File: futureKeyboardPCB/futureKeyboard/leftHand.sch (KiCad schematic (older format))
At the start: 56 parts, among them J10 Conn_01x02, J11 Conn_01x01, J12 Conn_01x01, J13 Conn_01x04, J14 Conn_01x06, J15 Conn_01x06, J16 Conn_01x01, J9 Conn_01x01, P3 CONN_01X02, P4 CONN_01X06, Q4 2SC1815, Q5 2SC1815, Q6 2SC1815, SW10 SW_Push, SW11 SW_Push, SW12 SW_Push, SW13 SW_Push, SW14 SW_Push, SW15 SW_Push, SW16 SW_Push, SW17 SW_Push, SW18 SW_Push, SW19 SW_Push, SW20 SW_Push, SW21 SW_Push, SW22 SW_Push, SW23 SW_Push, SW24 SW_Push, SW25 SW_Push, SW9 SW_SPDT, U3 AMS1117-1.5, U4 ESP32

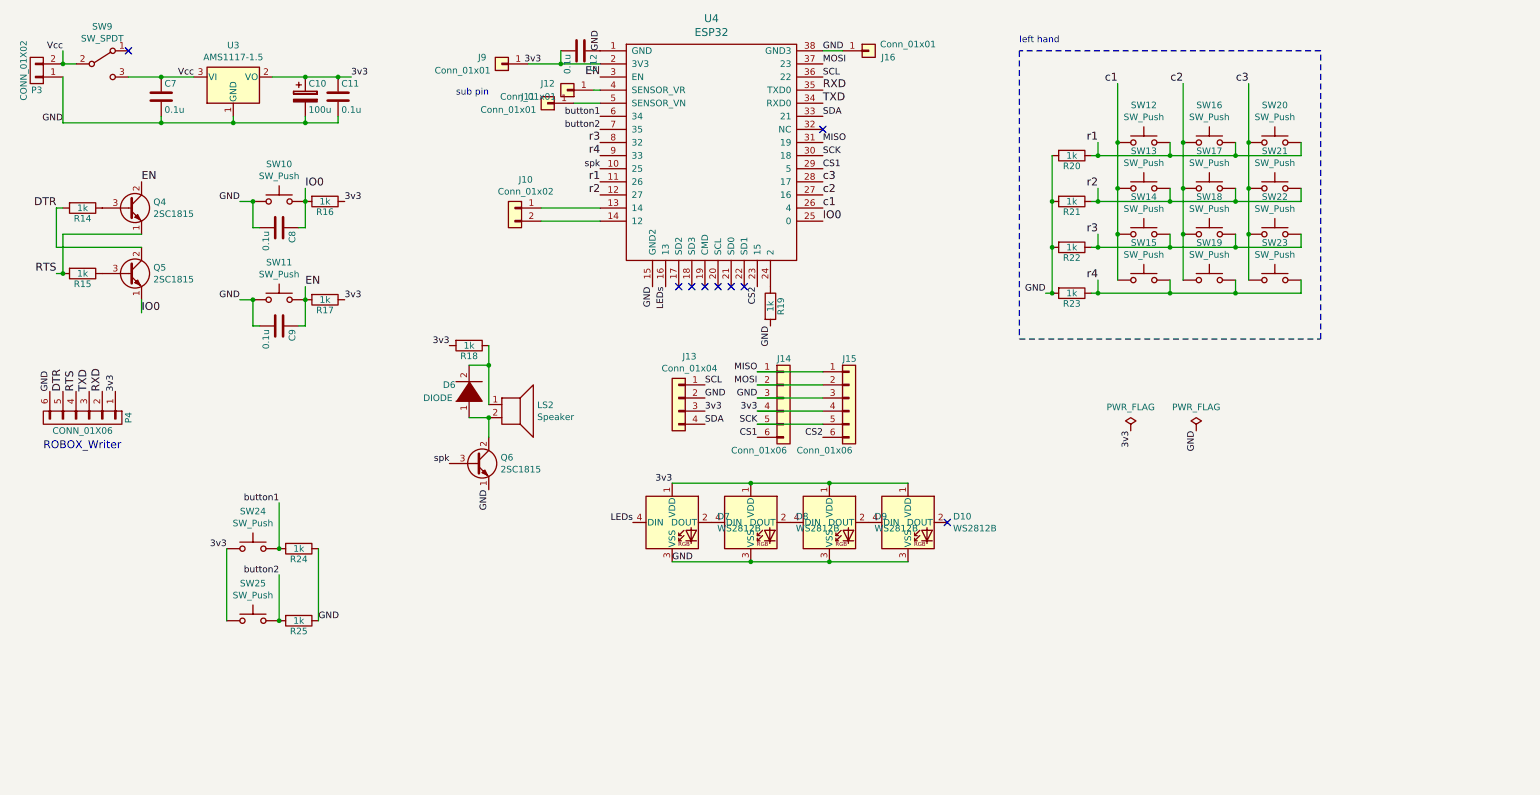
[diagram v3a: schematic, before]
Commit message: divide layors, make footprints, aligned footprints
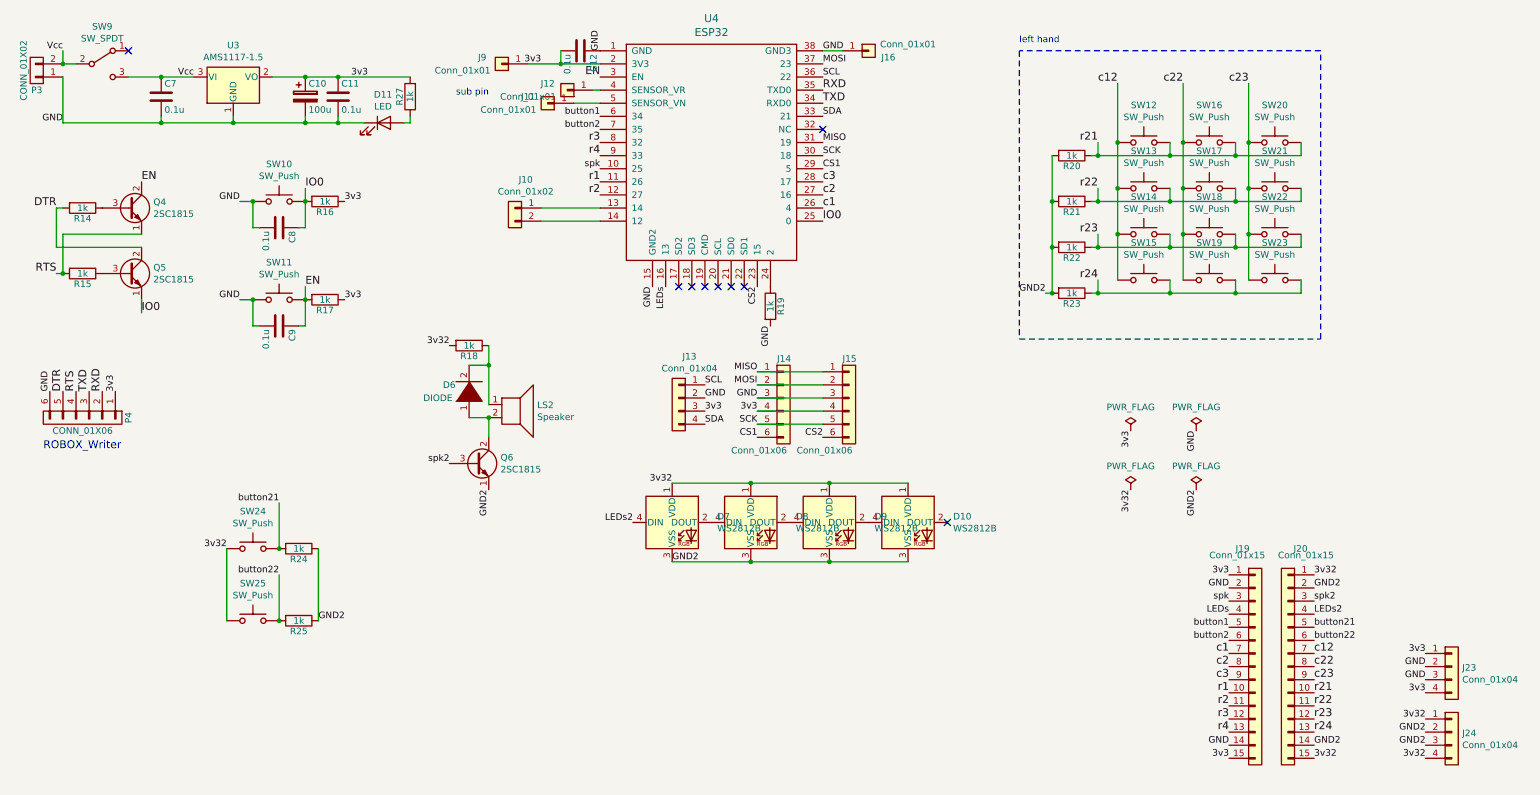
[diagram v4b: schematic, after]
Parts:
- added D11: LED, akizukit:2012LED, symbol Device:LED
- added J19, J20: Conn_01x15, Connector_PinHeader_2.54mm:PinHeader_1x15_P2.54mm_Vertical_SMD_Pin1Left, symbol Connector_Generic:Conn_01x15
- added J23, J24: Conn_01x04, Connector_PinHeader_2.54mm:PinHeader_1x04_P2.54mm_Vertical_SMD_Pin1Left, symbol Connector_Generic:Conn_01x04
- added R27: 1k, akizukit:SMD-1608, symbol Hyper_Board_Traser-rescue:R
- D10, D7, D8, D9: footprint LED_SMD:LED_WS2812B_PLCC4_5.0x5.0mm_P3.2mm -> akizukit:WS2812B
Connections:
- net 3v3: now also J19.1 (Pin_1), J19.15 (Pin_15), J23.1 (Pin_1), J23.4 (Pin_4), R27.2; no longer D10.1 (VDD), D7.1 (VDD), D8.1 (VDD), D9.1 (VDD), R18.2, SW24.1, SW25.1
- net GND: now also D11.1 (K), J19.14 (Pin_14), J19.2 (Pin_2), J23.2 (Pin_2), J23.3 (Pin_3); no longer D10.3 (VSS), D7.3 (VSS), D8.3 (VSS), D9.3 (VSS), Q6.1 (E), R20.2, R21.2, R22.2, R23.2, R24.1, R25.1
- net LEDs: now also J19.4 (Pin_4); no longer D7.4 (DIN)
- net button1: now also J19.5 (Pin_5); no longer R24.2, SW24.2
- net button2: now also J19.6 (Pin_6); no longer R25.2, SW25.2
- net c1: now also J19.7 (Pin_7); no longer SW12.1, SW13.1, SW14.1, SW15.1
- net c2: now also J19.8 (Pin_8); no longer SW16.1, SW17.1, SW18.1, SW19.1
- net c3: now also J19.9 (Pin_9); no longer SW20.1, SW21.1, SW22.1, SW23.1
- net r1: now also J19.10 (Pin_10); no longer R20.1, SW12.2, SW16.2, SW20.2
- net r2: now also J19.11 (Pin_11); no longer R21.1, SW13.2, SW17.2, SW21.2
- net r3: now also J19.12 (Pin_12); no longer R22.1, SW14.2, SW18.2, SW22.2
- net r4: now also J19.13 (Pin_13); no longer R23.1, SW15.2, SW19.2, SW23.2
- net spk: now also J19.3 (Pin_3); no longer Q6.3 (B)
- new net: D11.2 (A), R27.1
- new net 3v32: D10.1 (VDD), D7.1 (VDD), D8.1 (VDD), D9.1 (VDD), J20.1 (Pin_1), J20.15 (Pin_15), J24.1 (Pin_1), J24.4 (Pin_4), R18.2, SW24.1, SW25.1
- new net GND2: D10.3 (VSS), D7.3 (VSS), D8.3 (VSS), D9.3 (VSS), J20.14 (Pin_14), J20.2 (Pin_2), J24.2 (Pin_2), J24.3 (Pin_3), Q6.1 (E), R20.2, R21.2, R22.2, R23.2, R24.1, R25.1
- new net LEDs2: D7.4 (DIN), J20.4 (Pin_4)
- new net button21: J20.5 (Pin_5), R24.2, SW24.2
- new net button22: J20.6 (Pin_6), R25.2, SW25.2
- new net c12: J20.7 (Pin_7), SW12.1, SW13.1, SW14.1, SW15.1
- new net c22: J20.8 (Pin_8), SW16.1, SW17.1, SW18.1, SW19.1
- new net c23: J20.9 (Pin_9), SW20.1, SW21.1, SW22.1, SW23.1
- new net r21: J20.10 (Pin_10), R20.1, SW12.2, SW16.2, SW20.2
- new net r22: J20.11 (Pin_11), R21.1, SW13.2, SW17.2, SW21.2
- new net r23: J20.12 (Pin_12), R22.1, SW14.2, SW18.2, SW22.2
- new net r24: J20.13 (Pin_13), R23.1, SW15.2, SW19.2, SW23.2
- new net spk2: J20.3 (Pin_3), Q6.3 (B)
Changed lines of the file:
@@
 r1
 Text Label 10300 1200 2    60   ~ 0
-c3
+c23
 Text Label 9150 2350 2    60   ~ 0
-r3
+r23
 Text Label 9150 1650 2    60   ~ 0
-r1
+r21
 Text Label 9150 2700 2    60   ~ 0
-r4
+r24
 Text Label 9150 2000 2    60   ~ 0
-r2
-Text Label 9800 1200 2    60   ~ 0
-c2
-Text Label 9300 1200 2    60   ~ 0
-c1
+r22
 Wire Wire Line
 	9150 2000 9150 2100
@@
 c1
 Text Label 8750 2800 2    50   ~ 0
-GND
+GND2
 $Comp
 L Hyper_Board_Traser-rescue:C C?
@@
 $EndComp
 Text Label 4500 4300 3    50   ~ 0
-GND
+GND2
 Text Label 4200 3200 2    50   ~ 0
-3v3
+3v32
 $Comp
 L pspice:DIODE D?
@@
 spk
 Text Label 4200 4100 2    50   ~ 0
-spk
+spk2
 $Comp
 L LED:WS2812B D?
@@
 F 0 "D7" H 6244 4596 50  0000 L CNN
 F 1 "WS2812B" H 6244 4505 50  0000 L CNN
-F 2 "LED_SMD:LED_WS2812B_PLCC4_5.0x5.0mm_P3.2mm" H 5950 4250 50  0001 L TNN
+F 2 "akizukit:WS2812B" H 5950 4250 50  0001 L TNN
 F 3 "https://cdn-shop.adafruit.com/datasheets/WS2812B.pdf" H 6000 4175 50  0001 L TNN
 	1    5900 4550
@@
 $EndComp
 Text Label 5600 4550 2    50   ~ 0
-LEDs
+LEDs2
 Text Label 5900 4850 0    50   ~ 0
-GND
+GND2
 Text Label 5900 4250 2    50   ~ 0
-3v3
+3v32
 $Comp
 L LED:WS2812B D?
@@
 F 0 "D8" H 6844 4596 50  0000 L CNN
 F 1 "WS2812B" H 6844 4505 50  0000 L CNN
-F 2 "LED_SMD:LED_WS2812B_PLCC4_5.0x5.0mm_P3.2mm" H 6550 4250 50  0001 L TNN
+F 2 "akizukit:WS2812B" H 6550 4250 50  0001 L TNN
 F 3 "https://cdn-shop.adafruit.com/datasheets/WS2812B.pdf" H 6600 4175 50  0001 L TNN
 	1    6500 4550
@@
 F 0 "D9" H 7444 4596 50  0000 L CNN
 F 1 "WS2812B" H 7444 4505 50  0000 L CNN
-F 2 "LED_SMD:LED_WS2812B_PLCC4_5.0x5.0mm_P3.2mm" H 7150 4250 50  0001 L TNN
+F 2 "akizukit:WS2812B" H 7150 4250 50  0001 L TNN
 F 3 "https://cdn-shop.adafruit.com/datasheets/WS2812B.pdf" H 7200 4175 50  0001 L TNN
 	1    7100 4550
@@
 F 0 "D10" H 8044 4596 50  0000 L CNN
 F 1 "WS2812B" H 8044 4505 50  0000 L CNN
-F 2 "LED_SMD:LED_WS2812B_PLCC4_5.0x5.0mm_P3.2mm" H 7750 4250 50  0001 L TNN
+F 2 "akizukit:WS2812B" H 7750 4250 50  0001 L TNN
 F 3 "https://cdn-shop.adafruit.com/datasheets/WS2812B.pdf" H 7800 4175 50  0001 L TNN
 	1    7700 4550
@@
 $EndComp
 Text Label 2900 4400 2    50   ~ 0
-button1
+button21
 Text Label 2900 4950 2    50   ~ 0
-button2
+button22
 Text Label 2500 4750 2    50   ~ 0
-3v3
+3v32
 $Comp
 L Switch:SW_Push SW?
@@
 	3200 4750 3200 5300
 Text Label 3200 5300 0    50   ~ 0
-GND
+GND2
 Wire Wire Line
 	7200 950  7050 950
@@
 Connection ~ 3350 1150
 Wire Wire Line
-	3350 1150 3450 1150
-Wire Wire Line
 	2000 1150 2250 1150
 Wire Wire Line
@@
 P 9900 3850
 AR Path="/5F8C9354" Ref="#FLG?"  Part="1"
-AR Path="/5F548F89/5F8C9354" Ref="#FLG?"  Part="1"
-F 0 "#FLG?" H 9900 3945 50  0001 C CNN
+AR Path="/5F548F89/5F8C9354" Ref="#FLG0104"  Part="1"
+F 0 "#FLG0104" H 9900 3945 50  0001 C CNN
 F 1 "PWR_FLAG" H 9900 4030 50  0000 C CNN
 F 2 "" H 9900 3850 50  0000 C CNN
@@
 	1    0    0    -1
 $EndComp
+Text Label 10800 5350 0    50   ~ 0
+button21
+Text Label 10800 5050 0    50   ~ 0
+GND2
+Text Label 10800 5450 0    50   ~ 0
+button22
+Text Label 10800 4950 0    50   ~ 0
+3v32
+Text Label 10800 5250 0    50   ~ 0
+LEDs2
+Text Label 10800 5750 0    60   ~ 0
+c23
+Text Label 9300 1200 2    60   ~ 0
+c12
+Text Label 9800 1200 2    60   ~ 0
+c22
+Text Label 10800 5650 0    60   ~ 0
+c22
+Text Label 10800 5550 0    60   ~ 0
+c12
+Text Label 10800 6050 0    60   ~ 0
+r23
+Text Label 10800 5850 0    60   ~ 0
+r21
+Text Label 10800 6150 0    60   ~ 0
+r24
+Text Label 10800 5950 0    60   ~ 0
+r22
+Text Label 9400 4300 3    50   ~ 0
+3v32
+$Comp
+L Hyper_Board_Traser-rescue:PWR_FLAG #FLG?
+U 1 1 5F964A52
+P 9400 4300
+AR Path="/5F964A52" Ref="#FLG?"  Part="1"
+AR Path="/5F548F89/5F964A52" Ref="#FLG01"  Part="1"
+F 0 "#FLG01" H 9400 4395 50  0001 C CNN
+F 1 "PWR_FLAG" H 9400 4480 50  0000 C CNN
+F 2 "" H 9400 4300 50  0000 C CNN
+F 3 "" H 9400 4300 50  0000 C CNN
+	1    9400 4300
+	1    0    0    -1
+$EndComp
+Text Label 9900 4300 3    50   ~ 0
+GND2
+$Comp
+L Hyper_Board_Traser-rescue:PWR_FLAG #FLG?
+U 1 1 5F964A59
+P 9900 4300
+AR Path="/5F964A59" Ref="#FLG?"  Part="1"
+AR Path="/5F548F89/5F964A59" Ref="#FLG02"  Part="1"
+F 0 "#FLG02" H 9900 4395 50  0001 C CNN
+F 1 "PWR_FLAG" H 9900 4480 50  0000 C CNN
+F 2 "" H 9900 4300 50  0000 C CNN
+F 3 "" H 9900 4300 50  0000 C CNN
+	1    9900 4300
+	1    0    0    -1
+$EndComp
+Text Label 10800 5150 0    50   ~ 0
+spk2
+Text Label 10800 6250 0    50   ~ 0
+GND2
+Text Label 10800 6350 0    50   ~ 0
+3v32
+$Comp
+L Connector_Generic:Conn_01x15 J20
+U 1 1 5F97DF71
+P 10600 5650
+F 0 "J20" H 10450 6550 50  0000 L CNN
+F 1 "Conn_01x15" H 10250 6500 50  0000 L CNN
+F 2 "Connector_PinHeader_2.54mm:PinHeader_1x15_P2.54mm_Vertical_SMD_Pin1Left" H 10600 5650 50  0001 C CNN
+F 3 "~" H 10600 5650 50  0001 C CNN
+	1    10600 5650
+	-1   0    0    -1
+$EndComp
+$Comp
+L Connector_Generic:Conn_01x15 J19
+U 1 1 5F98488D
+P 10350 5650
+F 0 "J19" H 10200 6550 50  0000 L CNN
+F 1 "Conn_01x15" H 10000 6500 50  0000 L CNN
+F 2 "Connector_PinHeader_2.54mm:PinHeader_1x15_P2.54mm_Vertical_SMD_Pin1Left" H 10350 5650 50  0001 C CNN
+F 3 "~" H 10350 5650 50  0001 C CNN
+	1    10350 5650
+	1    0    0    -1
+$EndComp
+Text Label 10150 5250 2    50   ~ 0
+LEDs
+Text Label 10150 5050 2    50   ~ 0
+GND
+Text Label 10150 5650 2    60   ~ 0
+c2
+Text Label 10150 5550 2    60   ~ 0
+c1
+Text Label 10150 5750 2    60   ~ 0
+c3
+Text Label 10150 6050 2    60   ~ 0
+r3
+Text Label 10150 5850 2    60   ~ 0
+r1
+Text Label 10150 5950 2    60   ~ 0
+r2
+Text Label 10150 6150 2    60   ~ 0
+r4
+Text Label 10150 5150 2    50   ~ 0
+spk
+Text Label 10150 5350 2    50   ~ 0
+button1
+Text Label 10150 5450 2    50   ~ 0
+button2
+Text Label 10150 4950 2    50   ~ 0
+3v3
+Text Label 10150 6350 2    50   ~ 0
+3v3
+Text Label 10150 6250 2    50   ~ 0
+GND
+$Comp
+L Device:LED D11
+U 1 1 5F9C04FD
+P 3700 1500
+F 0 "D11" H 3693 1716 50  0000 C CNN
+F 1 "LED" H 3693 1625 50  0000 C CNN
+F 2 "akizukit:2012LED" H 3700 1500 50  0001 C CNN
+F 3 "~" H 3700 1500 50  0001 C CNN
+	1    3700 1500
+	1    0    0    -1
+$EndComp
+$Comp
+L Hyper_Board_Traser-rescue:R R?
+U 1 1 5F9C10E8
+P 3900 1300
+AR Path="/5F9C10E8" Ref="R?"  Part="1"
+AR Path="/5F548958/5F9C10E8" Ref="R?"  Part="1"
+AR Path="/5F548F89/5F9C10E8" Ref="R27"  Part="1"
+F 0 "R27" V 3980 1300 50  0000 C CNN
+F 1 "1k" V 3900 1300 50  0000 C CNN
+F 2 "akizukit:SMD-1608" V 3830 1300 50  0001 C CNN
+F 3 "" H 3900 1300 50  0000 C CNN
+	1    3900 1300
+	-1   0    0    1
+$EndComp
+Wire Wire Line
+	3550 1500 3350 1500
+Connection ~ 3350 1500
+Wire Wire Line
+	3850 1500 3900 1500
+Wire Wire Line
+	3900 1500 3900 1450
+Wire Wire Line
+	3350 1150 3900 1150
+$Comp
+L Connector_Generic:Conn_01x04 J?
+U 1 1 5F9DE2B0
+P 11850 5650
+AR Path="/5F548958/5F9DE2B0" Ref="J?"  Part="1"
+AR Path="/5F548F89/5F9DE2B0" Ref="J23"  Part="1"
+F 0 "J23" H 11930 5642 50  0000 L CNN
+F 1 "Conn_01x04" H 11930 5551 50  0000 L CNN
+F 2 "Connector_PinHeader_2.54mm:PinHeader_1x04_P2.54mm_Vertical_SMD_Pin1Left" H 11850 5650 50  0001 C CNN
+F 3 "~" H 11850 5650 50  0001 C CNN
+	1    11850 5650
+	1    0    0    -1
+$EndComp
+$Comp
+L Connector_Generic:Conn_01x04 J?
+U 1 1 5F9DE2B6
+P 11850 6150
+AR Path="/5F548958/5F9DE2B6" Ref="J?"  Part="1"
+AR Path="/5F548F89/5F9DE2B6" Ref="J24"  Part="1"
+F 0 "J24" H 11930 6142 50  0000 L CNN
+F 1 "Conn_01x04" H 11930 6051 50  0000 L CNN
+F 2 "Connector_PinHeader_2.54mm:PinHeader_1x04_P2.54mm_Vertical_SMD_Pin1Left" H 11850 6150 50  0001 C CNN
+F 3 "~" H 11850 6150 50  0001 C CNN
+	1    11850 6150
+	1    0    0    -1
+$EndComp
+Text Label 11650 5850 2    50   ~ 0
+3v3
+Text Label 11650 5650 2    50   ~ 0
+GND
+Text Label 11650 6150 2    50   ~ 0
+GND2
+Text Label 11650 6250 2    50   ~ 0
+GND2
+Text Label 11650 6350 2    50   ~ 0
+3v32
+Text Label 11650 5550 2    50   ~ 0
+3v3
+Text Label 11650 5750 2    50   ~ 0
+GND
+Text Label 11650 6050 2    50   ~ 0
+3v32
 $EndSCHEMATC

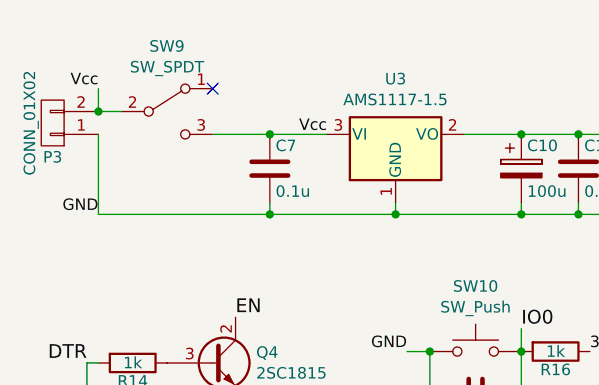
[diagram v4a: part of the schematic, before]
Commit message: fix circuit bags, and placement electric parts
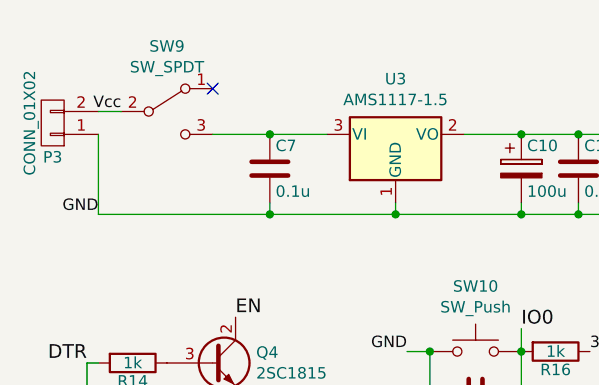
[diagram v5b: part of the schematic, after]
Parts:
- P4: footprint Connector_PinHeader_2.54mm:PinHeader_1x06_P2.54mm_Vertical -> Connector_PinHeader_2.54mm:PinHeader_1x06_P2.54mm_Horizontal
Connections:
- net Vcc: no longer C7.1, SW9.3 (C), U3.3 (VI)
- new net: C7.1, SW9.3 (C), U3.3 (VI)
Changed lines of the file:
@@
 F 0 "P4" H 1400 4100 50  0000 C CNN
 F 1 "CONN_01X06" V 1500 3750 50  0000 C CNN
-F 2 "Connector_PinHeader_2.54mm:PinHeader_1x06_P2.54mm_Vertical" H 1400 3750 50  0001 C CNN
+F 2 "Connector_PinHeader_2.54mm:PinHeader_1x06_P2.54mm_Horizontal" H 1400 3750 50  0001 C CNN
 F 3 "" H 1400 3750 50  0000 C CNN
 	1    1400 3750
@@
 Text Label 3450 1150 0    50   ~ 0
 3v3
-Text Label 1250 950  2    50   ~ 0
-Vcc
 Wire Wire Line
 	2000 1500 1250 1500
@@
 Wire Wire Line
 	1250 1150 1250 1500
-Wire Wire Line
-	1250 950  1250 1050
-Connection ~ 1250 1050
-Text Label 2250 1150 2    50   ~ 0
-Vcc
 $Comp
 L ume-boshi:AMS1117-1.5 U3
@@
 Text Label 11650 6050 2    50   ~ 0
 3v32
+Text Label 1350 1050 2    50   ~ 0
+Vcc
 $EndSCHEMATC

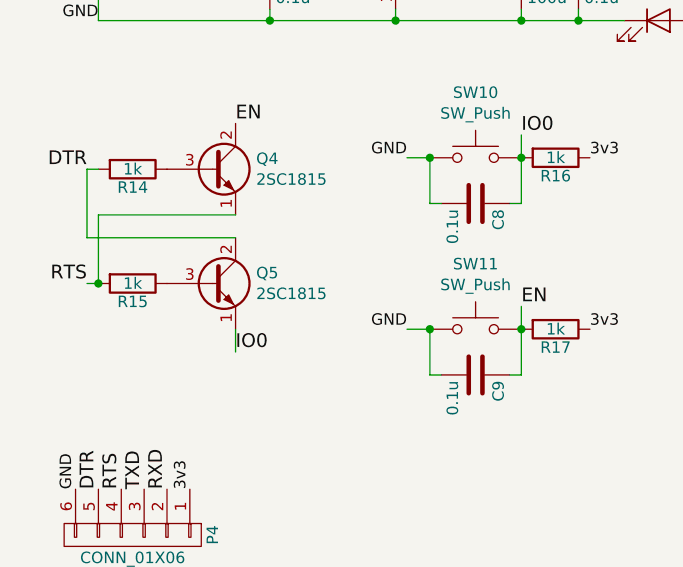
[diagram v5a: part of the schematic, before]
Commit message: complete placement electronic parts
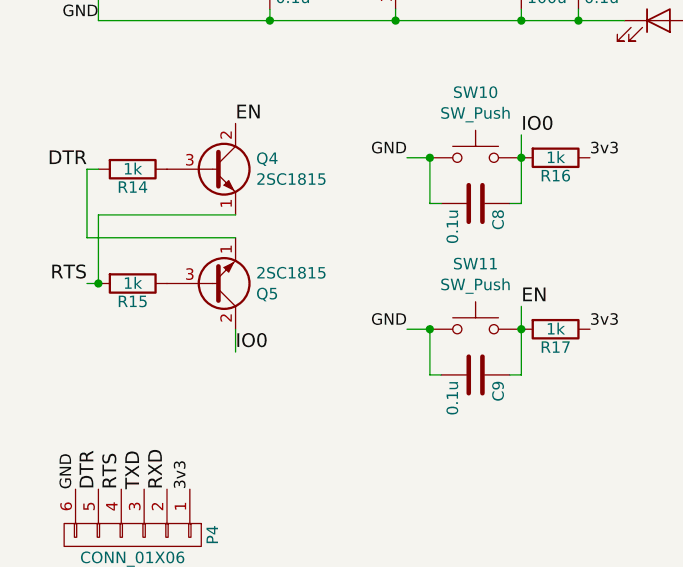
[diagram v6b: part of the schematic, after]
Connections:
- net DTR: now also Q5.1 (E); no longer Q5.2 (C)
- net IO0: now also Q5.2 (C); no longer Q5.1 (E)
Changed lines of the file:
@@
 F 3 "https://media.digikey.com/pdf/Data%20Sheets/Toshiba%20PDFs/2SC1815.pdf" H 1750 2650 50  0001 L CNN
 	1    1750 2650
-	1    0    0    -1
+	1    0    0    1
 $EndComp
 Text Label 1850 1950 0    60   ~ 0
